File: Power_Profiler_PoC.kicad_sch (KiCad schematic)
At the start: 0 parts

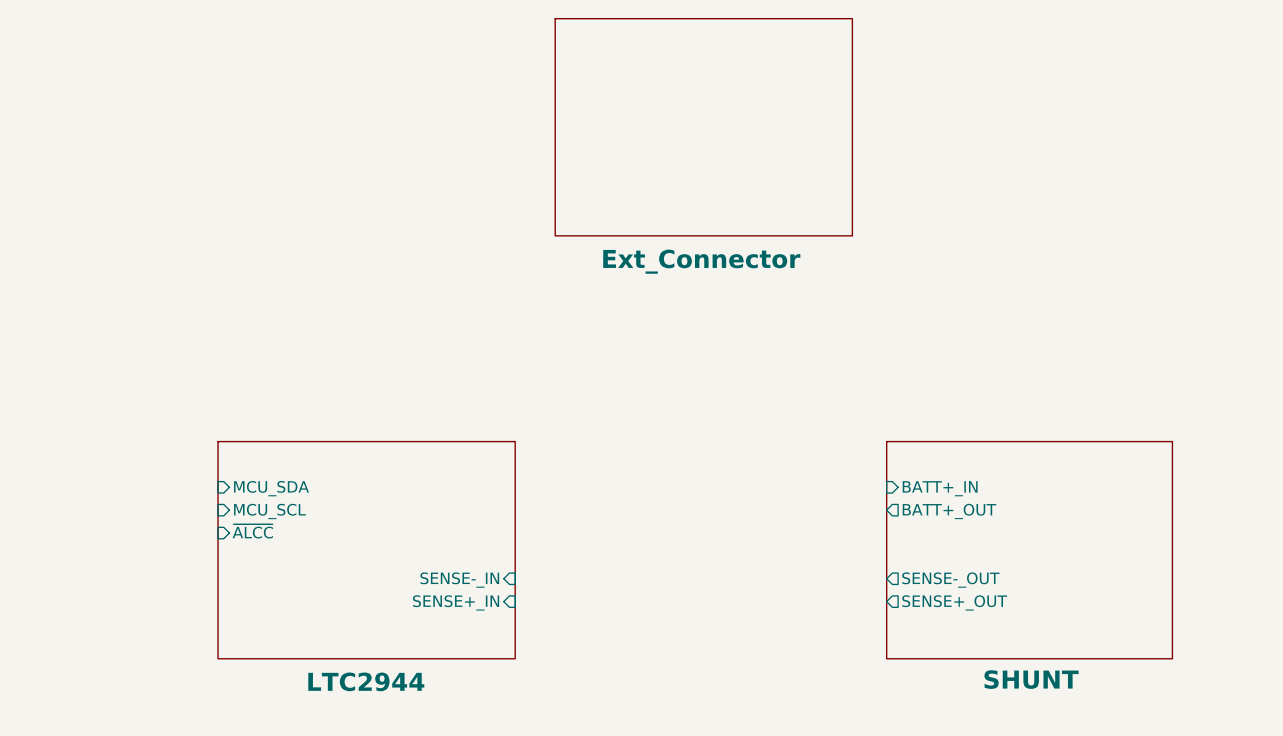
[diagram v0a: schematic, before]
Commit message: Assigned footprints
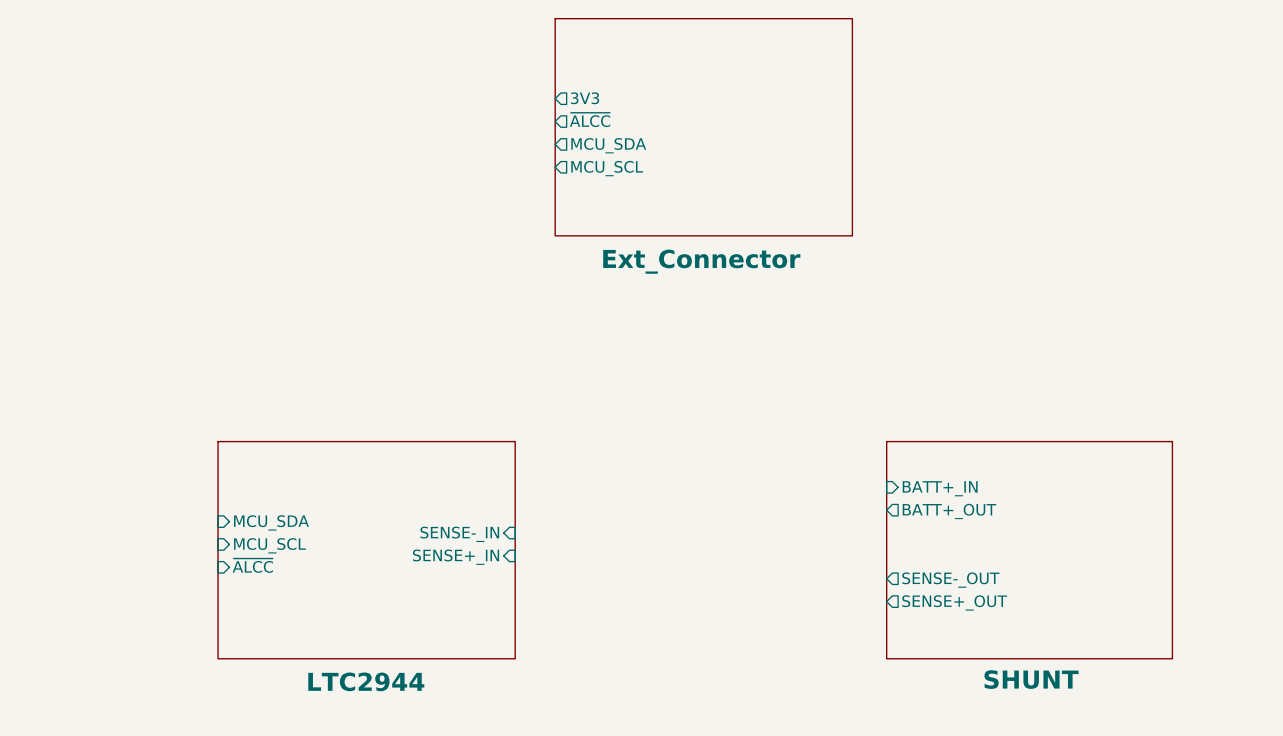
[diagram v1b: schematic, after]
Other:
- sheet Ext_Connector ports: added 3V3, MCU_SCL, MCU_SDA, ~{ALCC}; removed none
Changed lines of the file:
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@@
 		)
 		(pin "SENSE-_IN" input
-			(at 132.715 110.49 0)
+			(at 132.715 105.41 0)
 			(effects
 				(font
@@
 		)
 		(pin "SENSE+_IN" input
-			(at 132.715 113.03 0)
+			(at 132.715 107.95 0)
 			(effects
 				(font
@@
 		)
 		(pin "MCU_SDA" input
-			(at 99.695 100.33 180)
+			(at 99.695 104.14 180)
 			(effects
 				(font
@@
 		)
 		(pin "MCU_SCL" input
-			(at 99.695 102.87 180)
+			(at 99.695 106.68 180)
 			(effects
 				(font
@@
 		)
 		(pin "~{ALCC}" input
-			(at 99.695 105.41 180)
+			(at 99.695 109.22 180)
 			(effects
 				(font
@@
 			)
 		)
+		(pin "3V3" output
+			(at 137.16 57.15 180)
+			(effects
+				(font
+					(size 1.27 1.27)
+				)
+				(justify left)
+			)
+		)
+		(pin "~{ALCC}" output
+			(at 137.16 59.69 180)
+			(effects
+				(font
+					(size 1.27 1.27)
+				)
+				(justify left)
+			)
+		)
+		(pin "MCU_SDA" output
+			(at 137.16 62.23 180)
+			(effects
+				(font
+					(size 1.27 1.27)
+				)
+				(justify left)
+			)
+		)
+		(pin "MCU_SCL" output
+			(at 137.16 64.77 180)
+			(effects
+				(font
+					(size 1.27 1.27)
+				)
+				(justify left)
+			)
+		)

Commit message: Started routing
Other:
- sheet Ext_Connector ports: added BATT+_IN, BATT+_OUT, {SDA SCL ~{ALCC} 3V3/5V}; removed 3V3, MCU_SCL, MCU_SDA, ~{ALCC}
- sheet LTC2944 ports: added {SDA SCL ~{ALCC} 3V3/5V}; removed MCU_SCL, MCU_SDA, ~{ALCC}
- sheet SHUNT: file Shunt.kicad_sch -> SHUNT.kicad_sch
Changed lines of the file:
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@@
 		(comment 4 "Author: Vaibhav Khatri")
 	)
+	(bus
+		(pts
+			(xy 137.16 57.15) (xy 77.47 57.15)
+		)
+		(stroke
+			(width 0)
+			(type default)
+		)
+	)
+	(wire
+		(pts
+			(xy 205.74 96.52) (xy 205.74 62.23)
+		)
+		(stroke
+			(width 0.6)
+			(type default)
+		)
+	)
+	(bus
+		(pts
+			(xy 77.47 107.95) (xy 101.6 107.95)
+		)
+		(stroke
+			(width 0)
+			(type default)
+		)
+	)
+	(wire
+		(pts
+			(xy 201.93 64.77) (xy 201.93 96.52)
+		)
+		(stroke
+			(width 0.6)
+			(type default)
+		)
+	)
+	(wire
+		(pts
+			(xy 170.18 64.77) (xy 201.93 64.77)
+		)
+		(stroke
+			(width 0.6)
+			(type default)
+		)
+	)
+	(bus
+		(pts
+			(xy 77.47 57.15) (xy 77.47 107.95)
+		)
+		(stroke
+			(width 0)
+			(type default)
+		)
+	)
+	(wire
+		(pts
+			(xy 205.74 62.23) (xy 170.18 62.23)
+		)
+		(stroke
+			(width 0.6)
+			(type default)
+		)
+	)
+	(wire
+		(pts
+			(xy 142.24 110.49) (xy 173.99 110.49)
+		)
+		(stroke
+			(width 0.6)
+			(type default)
+		)
+	)
+	(wire
+		(pts
+			(xy 142.24 105.41) (xy 173.99 105.41)
+		)
+		(stroke
+			(width 0.6)
+			(type default)
+		)
+	)
+	(label "{SDA SCL ~{ALCC} 3V3{slash}5V}"
+		(at 106.68 57.15 0)
+		(fields_autoplaced yes)
+		(effects
+			(font
+				(size 1.27 1.27)
+			)
+			(justify left bottom)
+		)
+	)
 	(sheet
-		(at 99.695 95.25)
-		(size 33.02 24.13)
+		(at 101.6 96.52)
+		(size 40.64 24.13)
 		(stroke
 			(width 0.1524)
@@
 		)
 		(property "Sheetname" "LTC2944"
-			(at 109.474 123.19 0)
+			(at 116.078 124.968 0)
 			(effects
 				(font
 					(size 2 2)
 					(bold yes)
-					(color 0 0 255 1)
+					(color 0 0 0 1)
 				)
 				(justify left bottom)
@@
 		)
 		(property "Sheetfile" "LTC2944.kicad_sch"
-			(at 99.695 119.9646 0)
+			(at 101.6 121.2346 0)
 			(effects
 				(font
@@
 		)
 		(pin "SENSE-_IN" input
-			(at 132.715 105.41 0)
+			(at 142.24 105.41 0)
 			(effects
 				(font
@@
 		)
 		(pin "SENSE+_IN" input
-			(at 132.715 107.95 0)
-			(effects
-				(font
-					(size 1.27 1.27)
-				)
-				(justify right)
-			)
-		)
-		(pin "MCU_SDA" input
-			(at 99.695 104.14 180)
-			(effects
-				(font
-					(size 1.27 1.27)
-				)
-				(justify left)
-			)
-		)
-		(pin "MCU_SCL" input
-			(at 99.695 106.68 180)
-			(effects
-				(font
-					(size 1.27 1.27)
-				)
-				(justify left)
-			)
-		)
-		(pin "~{ALCC}" input
-			(at 99.695 109.22 180)
+			(at 142.24 110.49 0)
+			(effects
+				(font
+					(size 1.27 1.27)
+				)
+				(justify right)
+			)
+		)
+		(pin "{SDA SCL ~{ALCC} 3V3{slash}5V}" input
+			(at 101.6 107.95 180)
 			(effects
 				(font
@@
 	)
 	(sheet
-		(at 173.99 95.25)
-		(size 31.75 24.13)
+		(at 173.99 96.52)
+		(size 41.91 24.13)
 		(stroke
 			(width 0.1524)
@@
 		)
 		(property "Sheetname" "SHUNT"
-			(at 184.658 122.936 0)
+			(at 189.484 124.968 0)
 			(effects
 				(font
 					(size 2 2)
 					(bold yes)
-					(color 0 0 255 1)
+					(color 0 0 0 1)
 				)
 				(justify left bottom)
 			)
 		)
-		(property "Sheetfile" "Shunt.kicad_sch"
-			(at 173.99 119.9646 0)
+		(property "Sheetfile" "SHUNT.kicad_sch"
+			(at 173.99 121.2346 0)
 			(effects
 				(font
@@
 			)
 		)
+		(pin "SENSE+_OUT" output
+			(at 173.99 110.49 180)
+			(effects
+				(font
+					(size 1.27 1.27)
+				)
+				(justify left)
+			)
+		)
+		(pin "BATT+_OUT" output
+			(at 201.93 96.52 90)
+			(effects
+				(font
+					(size 1.27 1.27)
+				)
+				(justify right)
+			)
+		)
+		(pin "SENSE-_OUT" output
+			(at 173.99 105.41 180)
+			(effects
+				(font
+					(size 1.27 1.27)
+				)
+				(justify left)
+			)
+		)
 		(pin "BATT+_IN" input
-			(at 173.99 100.33 180)
-			(effects
-				(font
-					(size 1.27 1.27)
-				)
-				(justify left)
-			)
-		)
-		(pin "SENSE-_OUT" output
-			(at 173.99 110.49 180)
-			(effects
-				(font
-					(size 1.27 1.27)
-				)
-				(justify left)
-			)
-		)
-		(pin "SENSE+_OUT" output
-			(at 173.99 113.03 180)
-			(effects
-				(font
-					(size 1.27 1.27)
-				)
-				(justify left)
-			)
-		)
-		(pin "BATT+_OUT" output
-			(at 173.99 102.87 180)
-			(effects
-				(font
-					(size 1.27 1.27)
-				)
-				(justify left)
+			(at 205.74 96.52 90)
+			(effects
+				(font
+					(size 1.27 1.27)
+				)
+				(justify right)
 			)
 		)
@@
 			(project "Power_Profiler_PoC"
 				(path "/faeaf365-a06a-4014-84f4-b3c47881c674"
-					(page "3")
+					(page "4")
 				)
 			)
@@
 		)
 		(property "Sheetname" "Ext_Connector"
-			(at 142.24 76.2 0)
+			(at 144.018 75.692 0)
 			(effects
 				(font
 					(size 2 2)
 					(bold yes)
-					(color 0 0 255 1)
+					(color 0 0 0 1)
 				)
 				(justify left bottom)
@@
 			)
 		)
-		(pin "3V3" output
+		(pin "BATT+_OUT" input
+			(at 170.18 64.77 0)
+			(effects
+				(font
+					(size 1.27 1.27)
+				)
+				(justify right)
+			)
+		)
+		(pin "BATT+_IN" output
+			(at 170.18 62.23 0)
+			(effects
+				(font
+					(size 1.27 1.27)
+				)
+				(justify right)
+			)
+		)
+		(pin "{SDA SCL ~{ALCC} 3V3{slash}5V}" output
 			(at 137.16 57.15 180)
 			(effects
 				(font
-					(size 1.27 1.27)
-				)
-				(justify left)
-			)
-		)
-		(pin "~{ALCC}" output
-			(at 137.16 59.69 180)
-			(effects
-				(font
-					(size 1.27 1.27)
-				)
-				(justify left)
-			)
-		)
-		(pin "MCU_SDA" output
-			(at 137.16 62.23 180)
-			(effects
-				(font
-					(size 1.27 1.27)
-				)
-				(justify left)
-			)
-		)
-		(pin "MCU_SCL" output
-			(at 137.16 64.77 180)
-			(effects
-				(font
